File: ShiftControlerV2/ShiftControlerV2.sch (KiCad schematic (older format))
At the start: 21 parts, among them Q1 BTN8982TA

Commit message: Component value updates
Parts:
- R1, R5: renamed from R?; value R_Small -> 1k
- gave numbers to parts that had none: 18
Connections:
- net labels added: OUT1, OUT2
- wire segments 50 -> 52
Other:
- note added: "Bridge 1\n"
- note added: "Bridge 2\n\n"
- note removed: "1\n"
- note removed: "2\n\n"

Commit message: pcb detangled
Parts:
- added C11, C14: 10u, Capacitor_SMD:C_0201_0603Metric_Pad0.64x0.40mm_HandSolder, symbol Device:CP_Small
- added C12, C13: 10n, Capacitor_SMD:C_0201_0603Metric_Pad0.64x0.40mm_HandSolder, symbol Device:C_Small
- added J1: Conn_02x06_Counter_Clockwise, Lukas_Library:MX120G, symbol Connector_Generic:Conn_02x06_Counter_Clockwise
- added Q3, Q4: BSS138, digikey-footprints:SOT-23-3, symbol dk_Transistors-FETs-MOSFETs-Single:BSS138
- added R10, R11, R12, R9: 10k, Resistor_SMD:R_0201_0603Metric_Pad0.64x0.40mm_HandSolder, symbol Device:R_Small
- added U2: NCV7805BDTRKG, Package_TO_SOT_SMD:TO-252-3_TabPin4, symbol Lukas_Library:NCV7805BDTRKG
- C1, C10, C2, C3, C4, C5, C6, C7, C8, C9: footprint (none) -> Capacitor_SMD:C_0201_0603Metric_Pad0.64x0.40mm_HandSolder
- R1, R2, R3, R4, R5, R6, R7, R8: footprint (none) -> Resistor_SMD:R_0201_0603Metric_Pad0.64x0.40mm_HandSolder
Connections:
- net INH2 is gone; now on net +5V: R6.2
- net +12V: now also C11.1, C12.1, J1.1 (Pin_1), U2.1 (VI)
- net GND: now also C11.2, C12.2, C13.2, C14.2, J1.6 (Pin_6), U2.2 (GND), U2.4 (GND)
- net IN1: now also Q4.3 (D), R12.1
- net IN2: now also Q3.3 (D), R11.1
- net +3V3: now reaches U1.20 (+3v3)
- net +3V3: now also Q3.1 (G), Q4.1 (G), R10.2, R9.2
- net PB5: now reaches U1.30 (PB5)
- net PB5: now also Q4.2 (S), R10.1
- net PB4: now reaches U1.31 (PB4)
- net PB4: now also Q3.2 (S), R9.1
- net INH1 renamed +5V
- net +5V: now also C13.1, C14.1, R11.2, R12.2, U2.3 (VO)
- new net CANH: J1.12 (Pin_12)
- new net CANL: J1.11 (Pin_11)
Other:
- note added: "Logic Level Converter 1\n"
- note added: "Logic Level Converter 2"
- note added: "VREG"
- moved on the sheet: C1, C10, C2, C3, C4, C5, C6, C7, C8, C9, Q1, Q2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

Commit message: Schematic Revised
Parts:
- removed C11, C14: 10u, Capacitor_SMD:C_0201_0603Metric_Pad0.64x0.40mm_HandSolder, symbol Device:CP_Small
- removed C12, C13: 10n, Capacitor_SMD:C_0201_0603Metric_Pad0.64x0.40mm_HandSolder, symbol Device:C_Small
- removed Q3, Q4: BSS138, digikey-footprints:SOT-23-3, symbol dk_Transistors-FETs-MOSFETs-Single:BSS138
- removed R10, R11, R12, R9: 10k, Resistor_SMD:R_0201_0603Metric_Pad0.64x0.40mm_HandSolder, symbol Device:R_Small
- removed U2: NCV7805BDTRKG, Package_TO_SOT_SMD:TO-252-3_TabPin4, symbol Lukas_Library:NCV7805BDTRKG
- added C11: 1000u, Capacitor_THT:CP_Radial_D12.5mm_P5.00mm, symbol Device:C_Small
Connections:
- net +12V: now also C11.1
- net CANH: now also U1.18 (CANH)
- net CANL: now also U1.17 (CANL)
- net GND: now also C11.2
- net UARTRX: now reaches U1.22 (PA3)
- net UARTRX: now also J1.8 (Pin_8)
- net UARTTX: now reaches U1.23 (PA2)
- net UARTTX: now also J1.7 (Pin_7)
- net CURRENT1: now reaches U1.24 (PA1)
- net CURRENT2: now reaches U1.25 (PA0)
- net INH2: now reaches U1.28 (PB7)
- net INH2: now also R6.2
- net INH1: now reaches U1.29 (PB6)
- net INH1: now also R2.2
- removed net +5V: R2.2, R6.2
- no-connect marks 0 -> 22
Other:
- note added: "REG\n"
- note removed: "Logic Level Converter 1\n"
- note removed: "Logic Level Converter 2"
- note removed: "VREG"

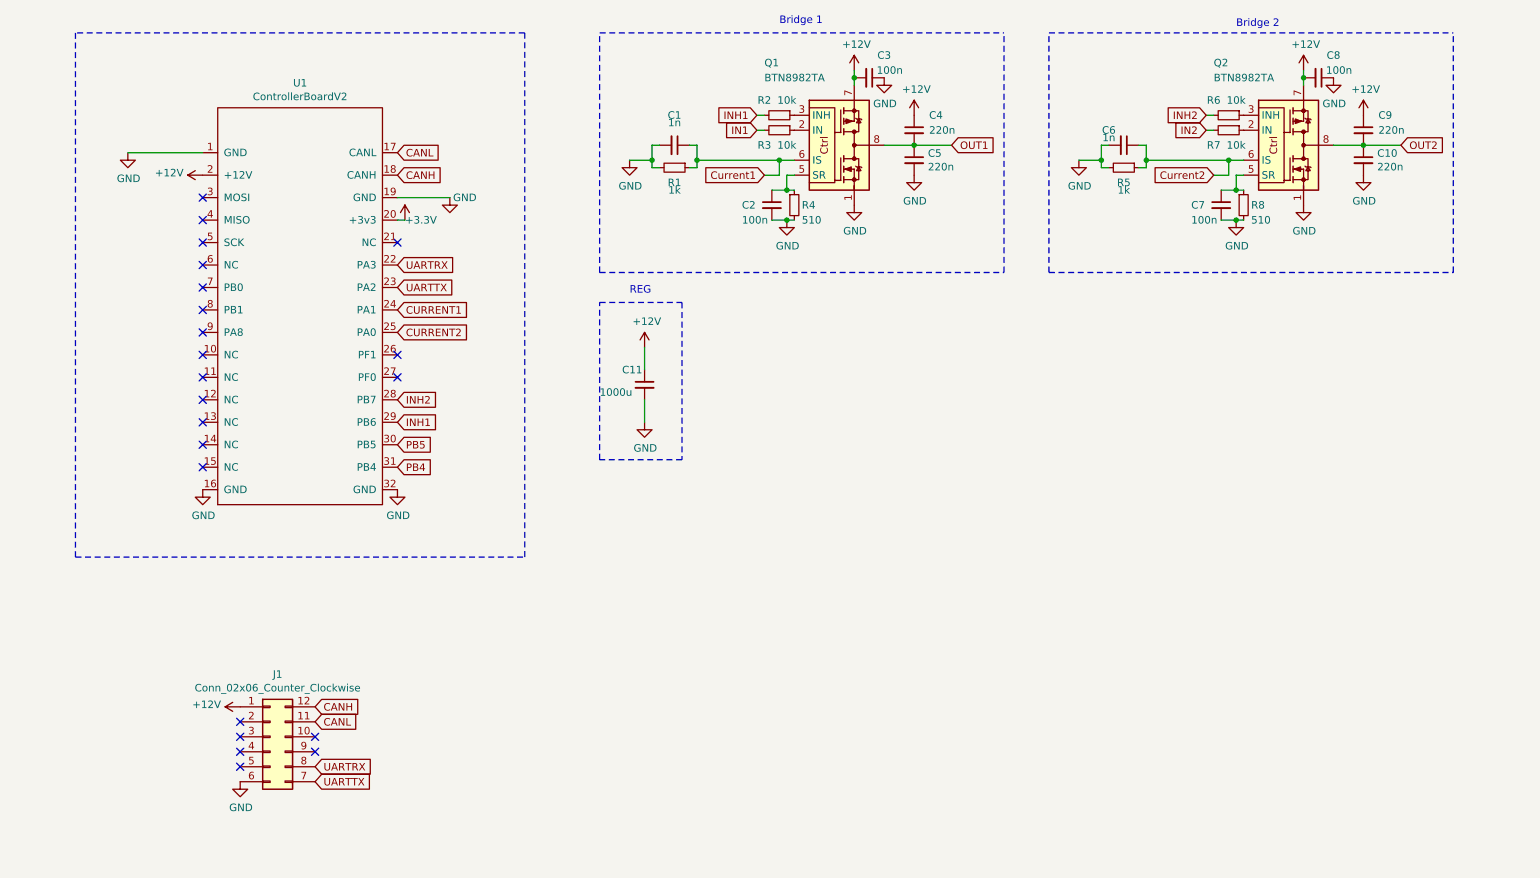
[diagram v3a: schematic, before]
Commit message: PCB Revised, Con Added
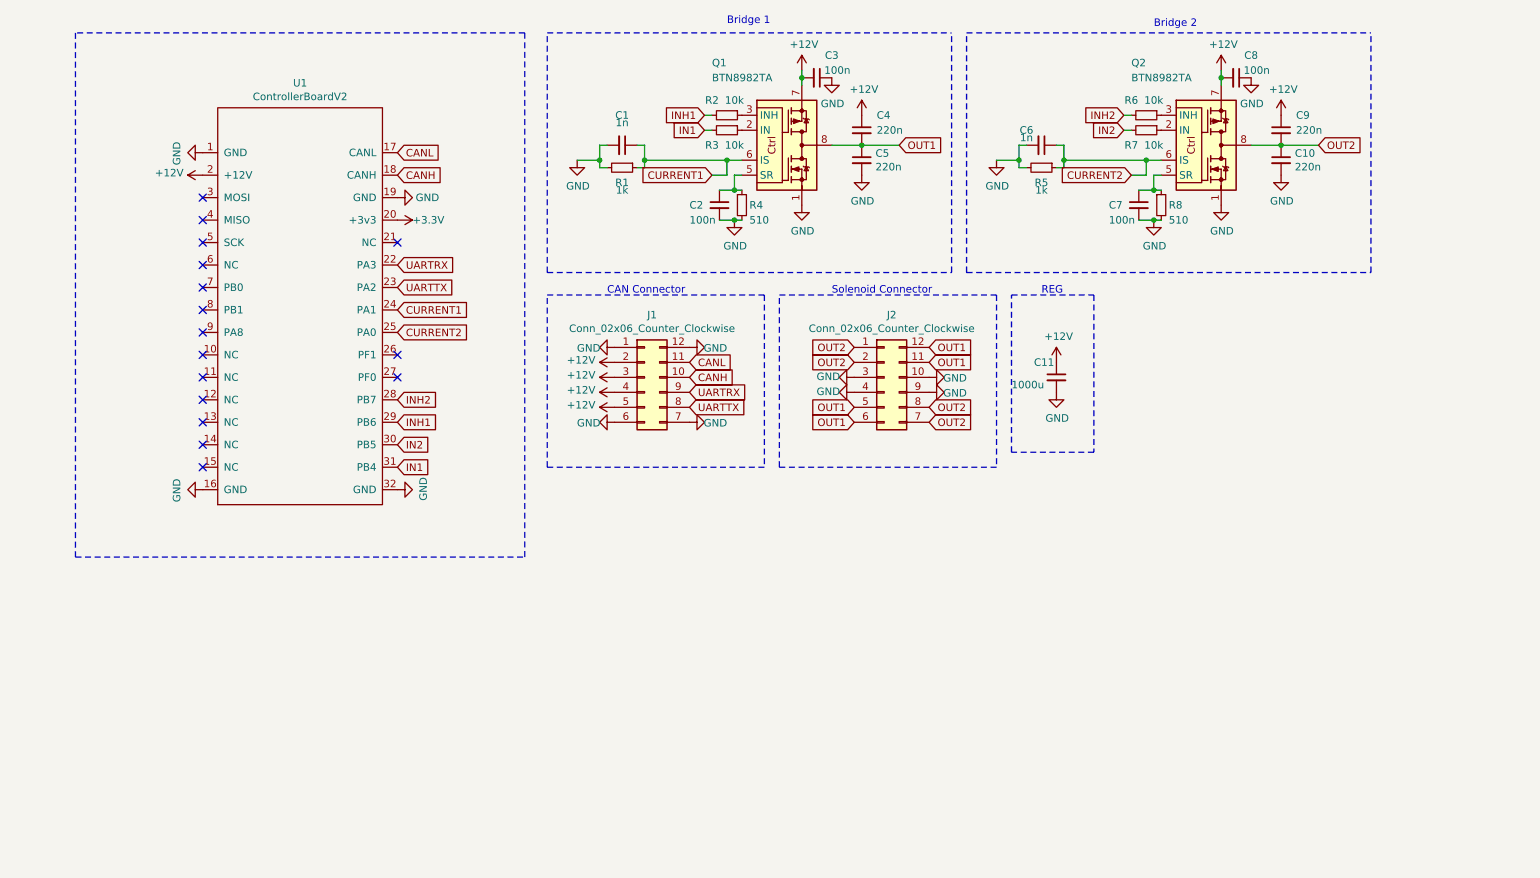
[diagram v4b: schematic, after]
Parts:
- added J2: Conn_02x06_Counter_Clockwise, Lukas_Library:MX120G, symbol Connector_Generic:Conn_02x06_Counter_Clockwise
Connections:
- net Current1 is gone; now on net CURRENT1: C1.1, Q1.6 (IS), R1.1
- net Current2 is gone; now on net CURRENT2: C6.1, Q2.6 (IS), R5.1
- net PB4 is gone; now on net IN1: U1.31 (PB4)
- net PB5 is gone; now on net IN2: U1.30 (PB5)
- net +12V: now also J1.2 (Pin_2), J1.3 (Pin_3), J1.4 (Pin_4), J1.5 (Pin_5); no longer J1.1 (Pin_1)
- net CANH: now also J1.10 (Pin_10); no longer J1.12 (Pin_12)
- net GND: now also J1.1 (Pin_1), J1.12 (Pin_12), J1.7 (Pin_7), J2.10 (Pin_10), J2.3 (Pin_3), J2.4 (Pin_4), J2.9 (Pin_9)
- net OUT1: now also J2.11 (Pin_11), J2.12 (Pin_12), J2.5 (Pin_5), J2.6 (Pin_6)
- net OUT2: now also J2.1 (Pin_1), J2.2 (Pin_2), J2.7 (Pin_7), J2.8 (Pin_8)
- net UARTRX: now also J1.9 (Pin_9); no longer J1.8 (Pin_8)
- net UARTTX: now also J1.8 (Pin_8); no longer J1.7 (Pin_7)
- no-connect marks 22 -> 16
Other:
- note added: "CAN Connector"
- note added: "Solenoid Connector\n"
- moved on the sheet: C1, C10, C11, C2, C3, C4, C5, C6, C7, C8, C9, J1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

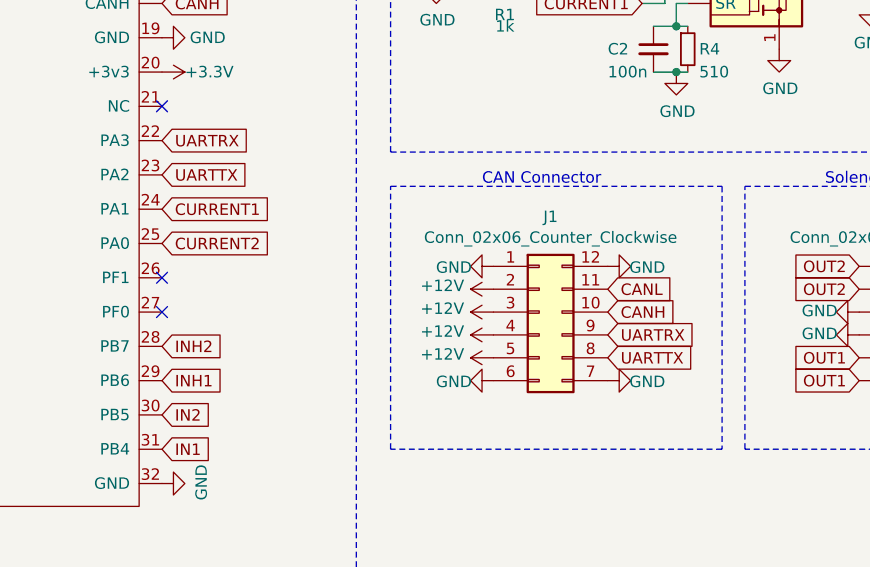
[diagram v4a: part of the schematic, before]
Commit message: Teeny tiny resistors
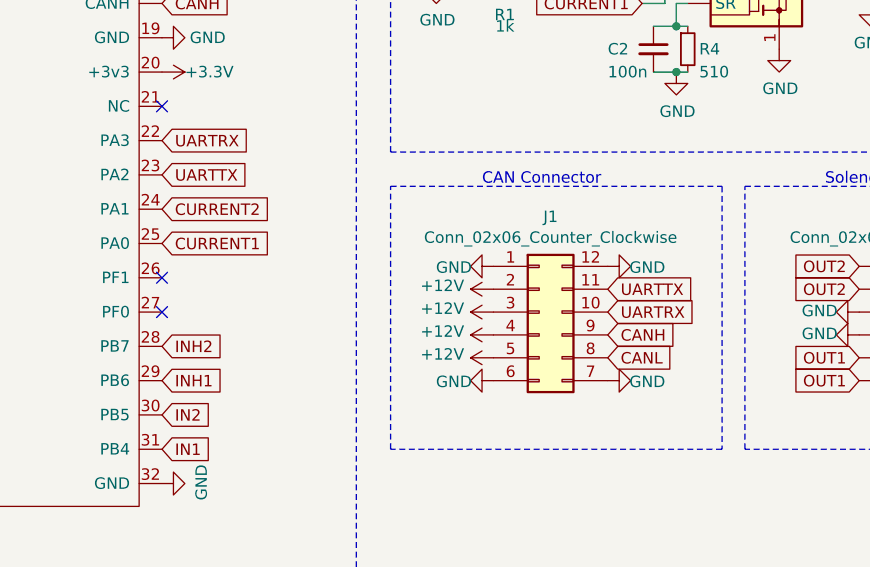
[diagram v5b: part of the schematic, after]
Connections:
- net CANH: now also J1.9 (Pin_9); no longer J1.10 (Pin_10)
- net CANL: now also J1.8 (Pin_8); no longer J1.11 (Pin_11)
- net CURRENT1: now also U1.25 (PA0); no longer U1.24 (PA1)
- net CURRENT2: now also U1.24 (PA1); no longer U1.25 (PA0)
- net UARTRX: now also J1.10 (Pin_10); no longer J1.9 (Pin_9)
- net UARTTX: now also J1.11 (Pin_11); no longer J1.8 (Pin_8)
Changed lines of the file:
@@
 	1    0    0    -1
 $EndComp
-Text GLabel 5100 3300 2    50   Input ~ 0
+Text GLabel 5100 3400 2    50   Input ~ 0
 CANH
-Text GLabel 5100 3200 2    50   Input ~ 0
+Text GLabel 5100 3500 2    50   Input ~ 0
 CANL
 $Comp
@@
 Text GLabel 3150 2700 2    50   Input ~ 0
 UARTTX
-Text GLabel 5100 3400 2    50   Input ~ 0
+Text GLabel 5100 3300 2    50   Input ~ 0
 UARTRX
-Text GLabel 5100 3500 2    50   Input ~ 0
+Text GLabel 5100 3200 2    50   Input ~ 0
 UARTTX
 Wire Notes Line
@@
 Text Notes 7450 2750 0    50   ~ 0
 REG\n
+Text GLabel 3150 3000 2    50   Input ~ 0
+CURRENT1
 Text GLabel 3150 2850 2    50   Input ~ 0
-CURRENT1
-Text GLabel 3150 3000 2    50   Input ~ 0
 CURRENT2
 NoConn ~ 3150 3150

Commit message: Rough Draft Finished
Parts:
- C1, C10, C2, C3, C4, C5, C6, C7, C8, C9: footprint Capacitor_SMD:C_0201_0603Metric_Pad0.64x0.40mm_HandSolder -> Capacitor_SMD:C_0603_1608Metric_Pad1.08x0.95mm_HandSolder
- R1, R2, R3, R4, R5, R6, R7, R8: footprint Resistor_SMD:R_0201_0603Metric_Pad0.64x0.40mm_HandSolder -> Resistor_SMD:R_0603_1608Metric_Pad0.98x0.95mm_HandSolder
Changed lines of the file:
@@
 F 0 "C3" V 5800 1400 50  0000 C CNN
 F 1 "100n" V 5900 1350 50  0000 L CNN
-F 2 "Capacitor_SMD:C_0201_0603Metric_Pad0.64x0.40mm_HandSolder" H 5950 1300 50  0001 C CNN
+F 2 "Capacitor_SMD:C_0603_1608Metric_Pad1.08x0.95mm_HandSolder" H 5950 1300 50  0001 C CNN
 F 3 "~" H 5950 1300 50  0001 C CNN
 	1    5950 1300
@@
 F 0 "C5" H 6342 1896 50  0000 L CNN
 F 1 "220n" H 6342 1805 50  0000 L CNN
-F 2 "Capacitor_SMD:C_0201_0603Metric_Pad0.64x0.40mm_HandSolder" H 6250 1850 50  0001 C CNN
+F 2 "Capacitor_SMD:C_0603_1608Metric_Pad1.08x0.95mm_HandSolder" H 6250 1850 50  0001 C CNN
 F 3 "~" H 6250 1850 50  0001 C CNN
 	1    6250 1850
@@
 F 0 "C4" H 6350 1750 50  0000 L CNN
 F 1 "220n" H 6350 1650 50  0000 L CNN
-F 2 "Capacitor_SMD:C_0201_0603Metric_Pad0.64x0.40mm_HandSolder" H 6250 1650 50  0001 C CNN
+F 2 "Capacitor_SMD:C_0603_1608Metric_Pad1.08x0.95mm_HandSolder" H 6250 1650 50  0001 C CNN
 F 3 "~" H 6250 1650 50  0001 C CNN
 	1    6250 1650
@@
 F 0 "R2" V 5250 1450 50  0000 C CNN
 F 1 "10k" V 5250 1600 50  0000 C CNN
-F 2 "Resistor_SMD:R_0201_0603Metric_Pad0.64x0.40mm_HandSolder" H 5350 1550 50  0001 C CNN
+F 2 "Resistor_SMD:R_0603_1608Metric_Pad0.98x0.95mm_HandSolder" H 5350 1550 50  0001 C CNN
 F 3 "~" H 5350 1550 50  0001 C CNN
 	1    5350 1550
@@
 F 0 "R3" V 5450 1550 50  0000 C CNN
 F 1 "10k" V 5450 1700 50  0000 C CNN
-F 2 "Resistor_SMD:R_0201_0603Metric_Pad0.64x0.40mm_HandSolder" H 5350 1650 50  0001 C CNN
+F 2 "Resistor_SMD:R_0603_1608Metric_Pad0.98x0.95mm_HandSolder" H 5350 1650 50  0001 C CNN
 F 3 "~" H 5350 1650 50  0001 C CNN
 	1    5350 1650
@@
 F 0 "R4" H 5500 2150 50  0000 L CNN
 F 1 "510" H 5500 2050 50  0000 L CNN
-F 2 "Resistor_SMD:R_0201_0603Metric_Pad0.64x0.40mm_HandSolder" H 5450 2150 50  0001 C CNN
+F 2 "Resistor_SMD:R_0603_1608Metric_Pad0.98x0.95mm_HandSolder" H 5450 2150 50  0001 C CNN
 F 3 "~" H 5450 2150 50  0001 C CNN
 	1    5450 2150
@@
 F 0 "C2" H 5100 2150 50  0000 L CNN
 F 1 "100n" H 5100 2050 50  0000 L CNN
-F 2 "Capacitor_SMD:C_0201_0603Metric_Pad0.64x0.40mm_HandSolder" H 5300 2150 50  0001 C CNN
+F 2 "Capacitor_SMD:C_0603_1608Metric_Pad1.08x0.95mm_HandSolder" H 5300 2150 50  0001 C CNN
 F 3 "~" H 5300 2150 50  0001 C CNN
 	1    5300 2150
@@
 F 0 "R1" V 4750 1900 50  0000 C CNN
 F 1 "1k" V 4800 1900 50  0000 C CNN
-F 2 "Resistor_SMD:R_0201_0603Metric_Pad0.64x0.40mm_HandSolder" H 4650 1900 50  0001 C CNN
+F 2 "Resistor_SMD:R_0603_1608Metric_Pad0.98x0.95mm_HandSolder" H 4650 1900 50  0001 C CNN
 F 3 "~" H 4650 1900 50  0001 C CNN
 	1    4650 1900
@@
 F 0 "C1" V 4450 1750 50  0000 C CNN
 F 1 "1n" V 4500 1750 50  0000 C CNN
-F 2 "Capacitor_SMD:C_0201_0603Metric_Pad0.64x0.40mm_HandSolder" H 4650 1750 50  0001 C CNN
+F 2 "Capacitor_SMD:C_0603_1608Metric_Pad1.08x0.95mm_HandSolder" H 4650 1750 50  0001 C CNN
 F 3 "~" H 4650 1750 50  0001 C CNN
 	1    4650 1750
@@
 F 0 "C8" V 8600 1400 50  0000 C CNN
 F 1 "100n" V 8700 1350 50  0000 L CNN
-F 2 "Capacitor_SMD:C_0201_0603Metric_Pad0.64x0.40mm_HandSolder" H 8750 1300 50  0001 C CNN
+F 2 "Capacitor_SMD:C_0603_1608Metric_Pad1.08x0.95mm_HandSolder" H 8750 1300 50  0001 C CNN
 F 3 "~" H 8750 1300 50  0001 C CNN
 	1    8750 1300
@@
 F 0 "C10" H 9142 1896 50  0000 L CNN
 F 1 "220n" H 9142 1805 50  0000 L CNN
-F 2 "Capacitor_SMD:C_0201_0603Metric_Pad0.64x0.40mm_HandSolder" H 9050 1850 50  0001 C CNN
+F 2 "Capacitor_SMD:C_0603_1608Metric_Pad1.08x0.95mm_HandSolder" H 9050 1850 50  0001 C CNN
 F 3 "~" H 9050 1850 50  0001 C CNN
 	1    9050 1850
@@
 F 0 "C9" H 9150 1750 50  0000 L CNN
 F 1 "220n" H 9150 1650 50  0000 L CNN
-F 2 "Capacitor_SMD:C_0201_0603Metric_Pad0.64x0.40mm_HandSolder" H 9050 1650 50  0001 C CNN
+F 2 "Capacitor_SMD:C_0603_1608Metric_Pad1.08x0.95mm_HandSolder" H 9050 1650 50  0001 C CNN
 F 3 "~" H 9050 1650 50  0001 C CNN
 	1    9050 1650
@@
 F 0 "R6" V 8050 1450 50  0000 C CNN
 F 1 "10k" V 8050 1600 50  0000 C CNN
-F 2 "Resistor_SMD:R_0201_0603Metric_Pad0.64x0.40mm_HandSolder" H 8150 1550 50  0001 C CNN
+F 2 "Resistor_SMD:R_0603_1608Metric_Pad0.98x0.95mm_HandSolder" H 8150 1550 50  0001 C CNN
 F 3 "~" H 8150 1550 50  0001 C CNN
 	1    8150 1550
@@
 F 0 "R7" V 8250 1550 50  0000 C CNN
 F 1 "10k" V 8250 1700 50  0000 C CNN
-F 2 "Resistor_SMD:R_0201_0603Metric_Pad0.64x0.40mm_HandSolder" H 8150 1650 50  0001 C CNN
+F 2 "Resistor_SMD:R_0603_1608Metric_Pad0.98x0.95mm_HandSolder" H 8150 1650 50  0001 C CNN
 F 3 "~" H 8150 1650 50  0001 C CNN
 	1    8150 1650
@@
 F 0 "R8" H 8300 2150 50  0000 L CNN
 F 1 "510" H 8300 2050 50  0000 L CNN
-F 2 "Resistor_SMD:R_0201_0603Metric_Pad0.64x0.40mm_HandSolder" H 8250 2150 50  0001 C CNN
+F 2 "Resistor_SMD:R_0603_1608Metric_Pad0.98x0.95mm_HandSolder" H 8250 2150 50  0001 C CNN
 F 3 "~" H 8250 2150 50  0001 C CNN
 	1    8250 2150
@@
 F 0 "C7" H 7900 2150 50  0000 L CNN
 F 1 "100n" H 7900 2050 50  0000 L CNN
-F 2 "Capacitor_SMD:C_0201_0603Metric_Pad0.64x0.40mm_HandSolder" H 8100 2150 50  0001 C CNN
+F 2 "Capacitor_SMD:C_0603_1608Metric_Pad1.08x0.95mm_HandSolder" H 8100 2150 50  0001 C CNN
 F 3 "~" H 8100 2150 50  0001 C CNN
 	1    8100 2150
@@
 F 0 "R5" V 7550 1900 50  0000 C CNN
 F 1 "1k" V 7600 1900 50  0000 C CNN
-F 2 "Resistor_SMD:R_0201_0603Metric_Pad0.64x0.40mm_HandSolder" H 7450 1900 50  0001 C CNN
+F 2 "Resistor_SMD:R_0603_1608Metric_Pad0.98x0.95mm_HandSolder" H 7450 1900 50  0001 C CNN
 F 3 "~" H 7450 1900 50  0001 C CNN
 	1    7450 1900
@@
 F 0 "C6" V 7350 1650 50  0000 C CNN
 F 1 "1n" V 7400 1650 50  0000 C CNN
-F 2 "Capacitor_SMD:C_0201_0603Metric_Pad0.64x0.40mm_HandSolder" H 7450 1750 50  0001 C CNN
+F 2 "Capacitor_SMD:C_0603_1608Metric_Pad1.08x0.95mm_HandSolder" H 7450 1750 50  0001 C CNN
 F 3 "~" H 7450 1750 50  0001 C CNN
 	1    7450 1750

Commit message: Design reviewed
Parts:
- C11: footprint Capacitor_THT:CP_Radial_D12.5mm_P5.00mm -> Capacitor_THT:CP_Radial_D12.5mm_P7.50mm
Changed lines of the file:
@@
 Sheet 1 1
 Title "ShiftController V2"
-Date ""
-Rev ""
-Comp ""
-Comment1 ""
+Date "2021-01-26"
+Rev "1"
+Comp "UBCO MotorSports"
+Comment1 "DB: Jacob N"
 Comment2 ""
 Comment3 ""
@@
 F 0 "C11" H 7400 3400 50  0000 L CNN
 F 1 "1000u" H 7250 3250 50  0000 L CNN
-F 2 "Capacitor_THT:CP_Radial_D12.5mm_P5.00mm" H 7550 3300 50  0001 C CNN
+F 2 "Capacitor_THT:CP_Radial_D12.5mm_P7.50mm" H 7550 3300 50  0001 C CNN
 F 3 "~" H 7550 3300 50  0001 C CNN
 	1    7550 3300
